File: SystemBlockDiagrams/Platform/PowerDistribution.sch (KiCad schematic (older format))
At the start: 1 part

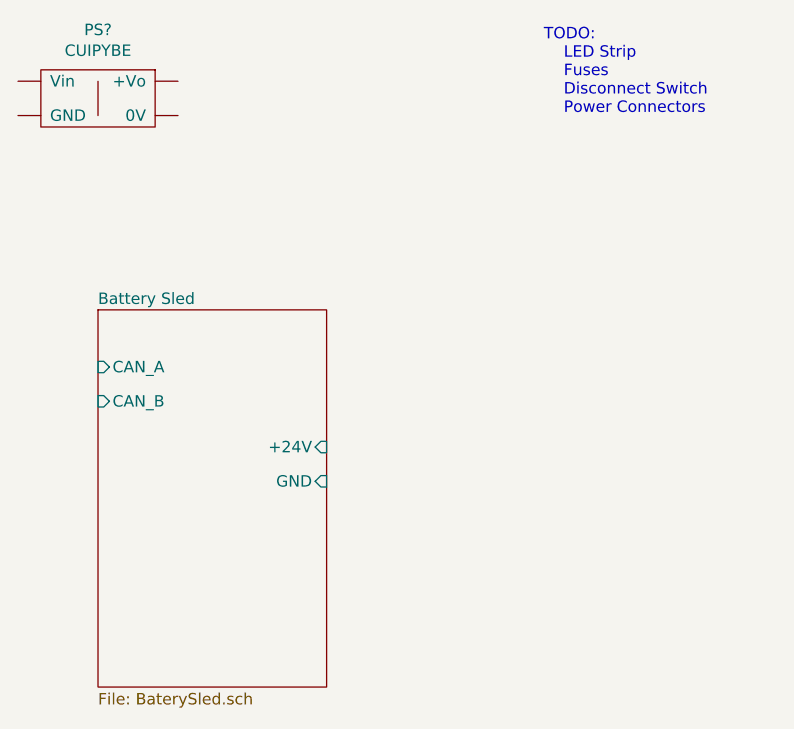
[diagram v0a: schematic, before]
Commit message: More platorm parts and connectors
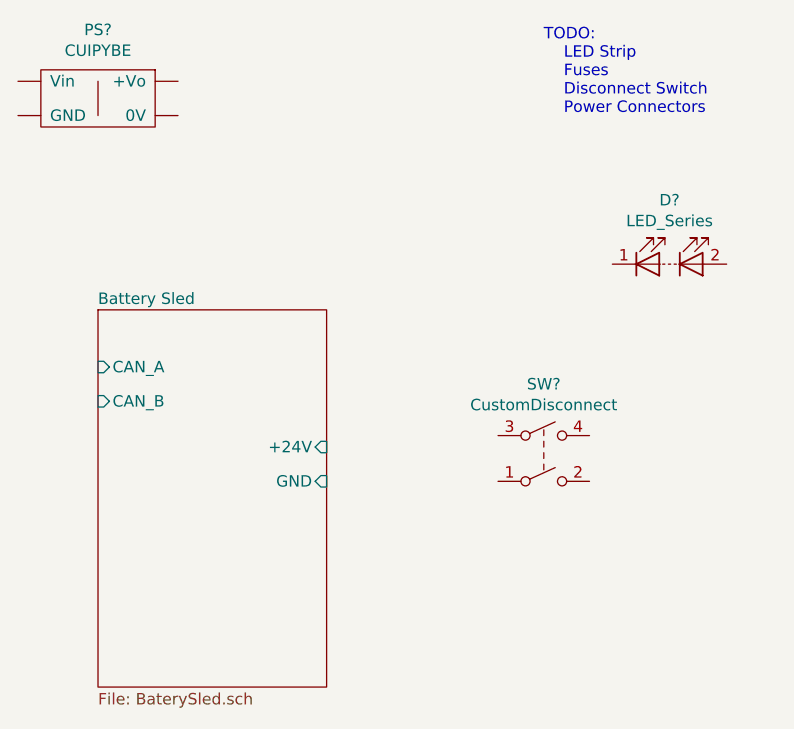
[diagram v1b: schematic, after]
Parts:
- added D?: LED_Series, symbol Device:LED_Series
- added SW?: CustomDisconnect, symbol Switch:SW_DPST
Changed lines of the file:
@@
 Text Notes 7050 1750 0    50   ~ 0
 TODO:\n    LED Strip\n    Fuses\n    Disconnect Switch\n    Power Connectors
+$Comp
+L Device:LED_Series D?
+U 1 1 5E280DCF
+P 7600 2400
+F 0 "D?" H 7600 2680 50  0000 C CNN
+F 1 "LED_Series" H 7600 2589 50  0000 C CNN
+F 2 "" H 7500 2400 50  0001 C CNN
+F 3 "~" H 7500 2400 50  0001 C CNN
+	1    7600 2400
+	1    0    0    -1
+$EndComp
+$Comp
+L Switch:SW_DPST SW?
+U 1 1 5E2817A6
+P 7050 3250
+F 0 "SW?" H 7050 3575 50  0000 C CNN
+F 1 "CustomDisconnect" H 7050 3484 50  0000 C CNN
+F 2 "" H 7050 3250 50  0001 C CNN
+F 3 "~" H 7050 3250 50  0001 C CNN
+F 4 "" H 7050 3250 50  0001 C CNN "Field4"
+	1    7050 3250
+	1    0    0    -1
+$EndComp
 $EndSCHEMATC

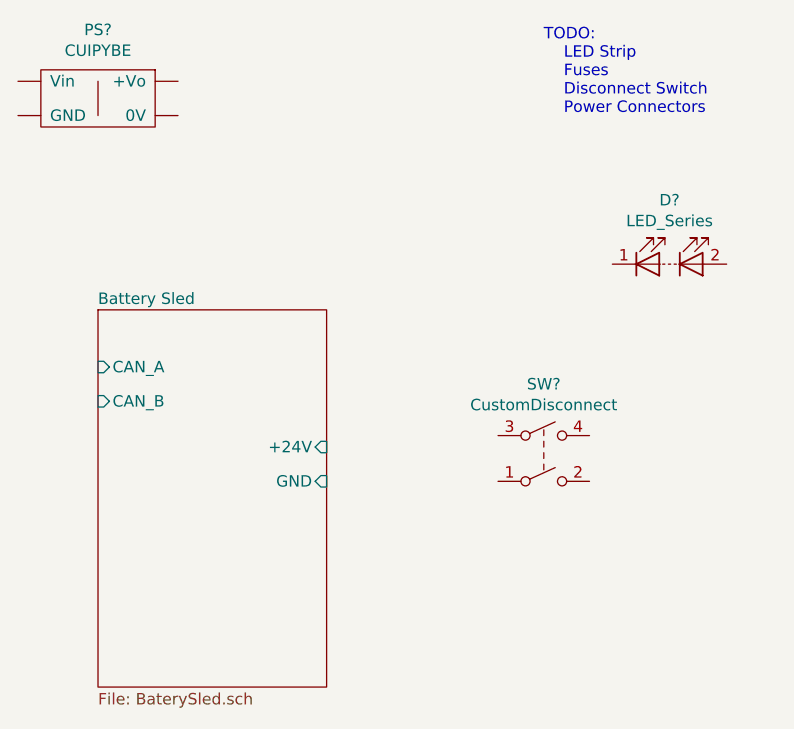
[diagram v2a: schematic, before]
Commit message: Update part numbers for BOM generation
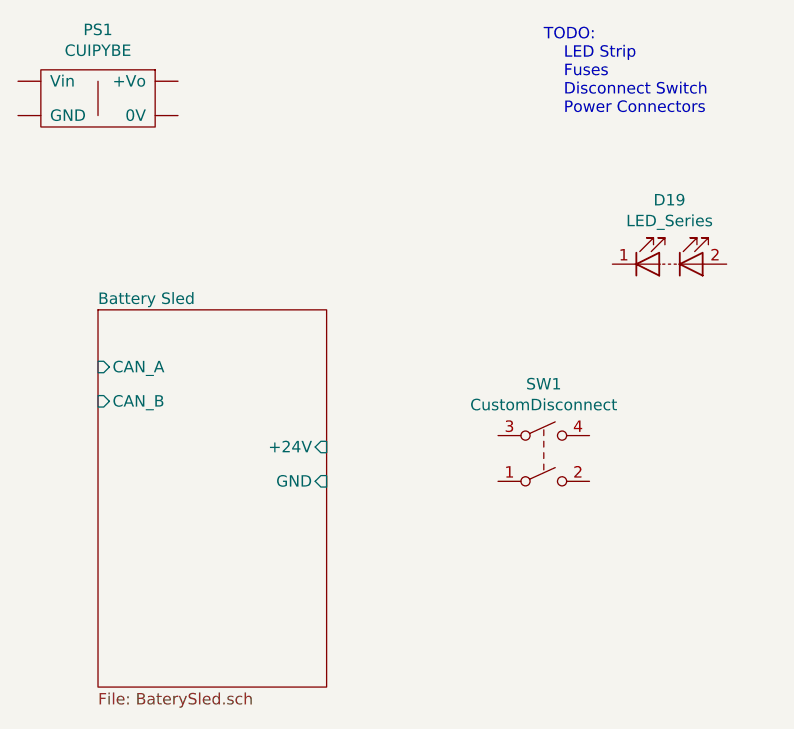
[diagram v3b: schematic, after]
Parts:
- PS1: renamed from PS?; Manufacturer (none) -> CUI Inc.; Manufacturer Part Number (none) -> PYBE30-Q24-S5-T; Supplier (none) -> Digi-Key; Supplier Part Number (none) -> 102-6025-ND
- SW1: renamed from SW?; Manufacturer (none) -> Jascha; Manufacturer Part Number (none) -> CHOMP-DISCONNECT; Supplier (none) -> Jascha; Supplier Part Number (none) -> CHOMP-DISCONNECT
- gave numbers to parts that had none: 1
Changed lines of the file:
@@
 $EndDescr
 $Comp
-L Stomp:CUIPYBE PS?
+L Stomp:CUIPYBE PS1
 U 1 1 5E26E04C
 P 5100 1700
-F 0 "PS?" H 5100 2025 50  0000 C CNN
+F 0 "PS1" H 5100 2025 50  0000 C CNN
 F 1 "CUIPYBE" H 5100 1934 50  0000 C CNN
 F 2 "" H 4900 1900 50  0001 C CNN
-F 3 "" H 4900 1900 50  0001 C CNN
+F 3 "https://www.cui.com/product/resource/digikeypdf/pybe30-t.pdf" H 4900 1900 50  0001 C CNN
+F 4 "CUI Inc." H 5100 1700 50  0001 C CNN "Manufacturer"
+F 5 "PYBE30-Q24-S5-T" H 5100 1700 50  0001 C CNN "Manufacturer Part Number"
+F 6 "Digi-Key" H 5100 1700 50  0001 C CNN "Supplier"
+F 7 "102-6025-ND" H 5100 1700 50  0001 C CNN "Supplier Part Number"
 	1    5100 1700
 	1    0    0    -1
@@
 TODO:\n    LED Strip\n    Fuses\n    Disconnect Switch\n    Power Connectors
 $Comp
-L Device:LED_Series D?
+L Device:LED_Series D19
 U 1 1 5E280DCF
 P 7600 2400
-F 0 "D?" H 7600 2680 50  0000 C CNN
+F 0 "D19" H 7600 2680 50  0000 C CNN
 F 1 "LED_Series" H 7600 2589 50  0000 C CNN
 F 2 "" H 7500 2400 50  0001 C CNN
@@
 $EndComp
 $Comp
-L Switch:SW_DPST SW?
+L Switch:SW_DPST SW1
 U 1 1 5E2817A6
 P 7050 3250
-F 0 "SW?" H 7050 3575 50  0000 C CNN
+F 0 "SW1" H 7050 3575 50  0000 C CNN
 F 1 "CustomDisconnect" H 7050 3484 50  0000 C CNN
 F 2 "" H 7050 3250 50  0001 C CNN
 F 3 "~" H 7050 3250 50  0001 C CNN
-F 4 "" H 7050 3250 50  0001 C CNN "Field4"
+F 4 "Jascha" H 7050 3250 50  0001 C CNN "Manufacturer"
+F 5 "CHOMP-DISCONNECT" H 7050 3250 50  0001 C CNN "Manufacturer Part Number"
+F 6 "Jascha" H 7050 3250 50  0001 C CNN "Supplier"
+F 7 "CHOMP-DISCONNECT" H 7050 3250 50  0001 C CNN "Supplier Part Number"
 	1    7050 3250
 	1    0    0    -1
